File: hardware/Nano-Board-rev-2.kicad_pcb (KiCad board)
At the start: 2 copper layers, 125.7 x 53 mm, 75 parts, among them J1 Conn_01x02_Pin, J2 USB_B_Micro, J3 Conn_02x05_Odd_Even, J4 Conn_02x05_Odd_Even, J5 Conn_02x05_Odd_Even, J6 Micro_SD_Card_Det1, P1 Conn_02x05_Odd_Even, P2 Conn_02x05_Odd_Even, P3 Conn_02x05_Odd_Even, U1 STM32F303CCTx, U4 CDSOT236-0504C, U5 TLV75733PDBV, U6 STLINK-V3MODS, U8 MPU6050, Y1 8MHz Crystal

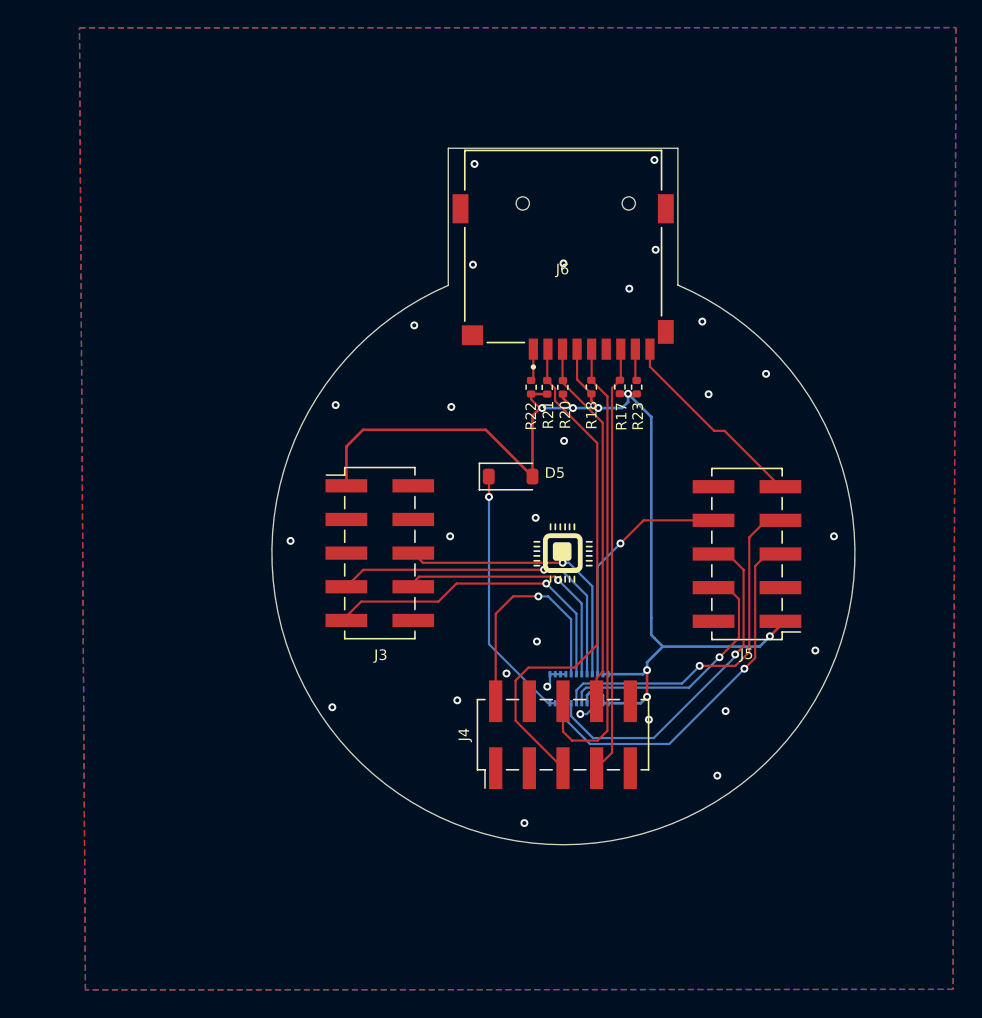
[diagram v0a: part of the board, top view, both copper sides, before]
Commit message: hardware: prune auxiliary libraries and refresh PCB
Delete vendor footprint/symbol bundles that were lying around
hardware/ as reference imports — none of them are used by
Nano-Board-rev-2.kicad_pcb directly:

  - 1x2_Hea/, FPC/, MPU-6050/, SAMTEC-SMH_1x2/,
    USB/, USB MICRO/, USB MICRO 4 NANO/, XKB_microSD.pretty/,
    fp/, stlink-v3mods_cad/
  - LDO/ sub-project (separate board, doesn't belong here)
  - one-off helpers: how-to-import.htm at various paths,
    fabrication-toolkit-options.json, nano (2).csv,
    Backup.gitignore.txt
  - cached pre-built 3D models under hardware/3d/ (KiCad regenerates
    them on demand)

The PCB itself is updated.
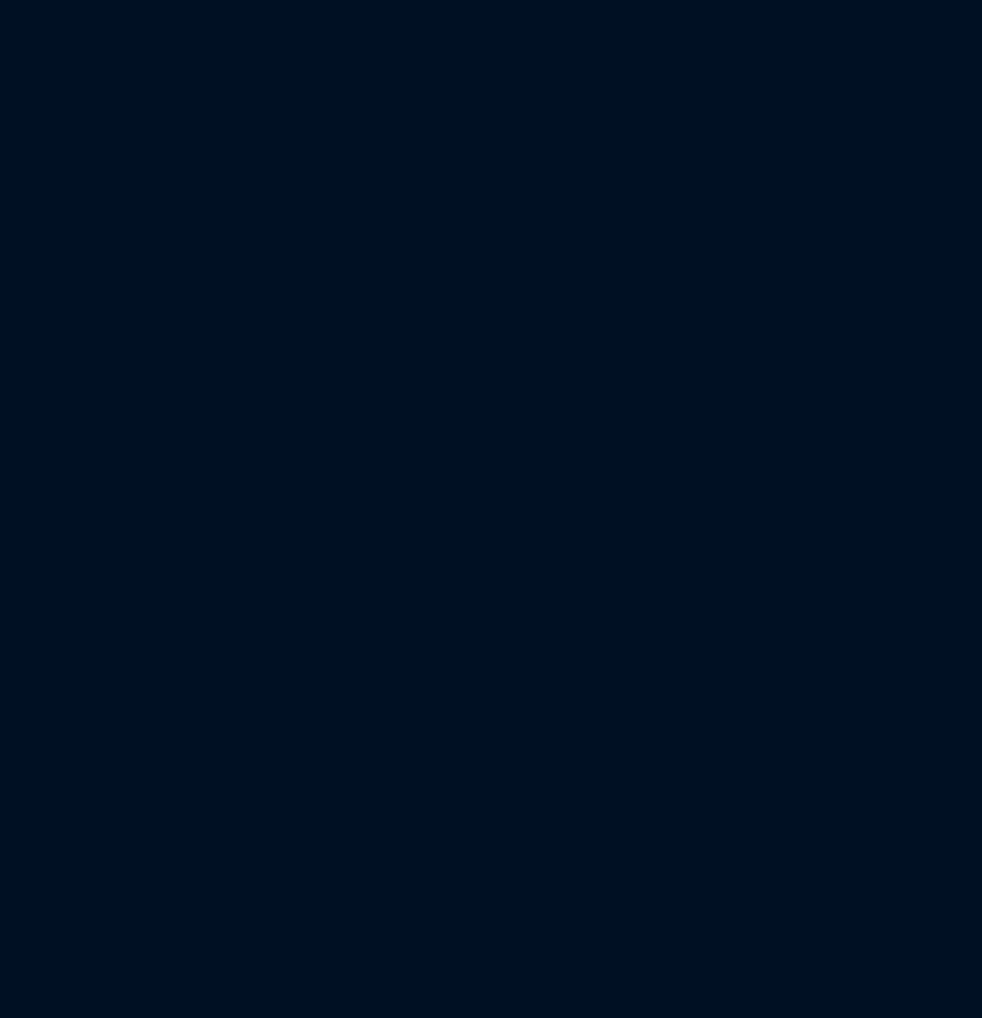
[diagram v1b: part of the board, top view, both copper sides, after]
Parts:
- removed D5: 1N5819WS, Diode_SMD:D_SOD-123
- removed the G*** at (177.5, 111.8)
- removed the G*** at (173.3, 83.4)
- removed J3, J4, J5: Conn_02x05_Odd_Even, Connector_PinHeader_2.54mm:PinHeader_2x05_P2.54mm_Vertical_SMD
- removed J6: Micro_SD_Card_Det1, fp:CUI_MSD-1-A
- removed R17, R18, R20, R21, R22, R23: 10K, Resistor_SMD:R_0402_1005Metric
- removed U3: ~, FPC_CONNECTOR24:OK-24F024-04
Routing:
- net +3.3V: track 86.3 -> 0.00 mm, vias 7 -> 0
- net SD_CS: track 39.2 -> 0.00 mm
- net SD_SCL: track 35.5 -> 0.00 mm
- net SD_MISO: track 32.2 -> 0.00 mm
- net TP_IN: track 28.2 -> 0.00 mm, vias 1 -> 0
- net SD_MOSI: track 28.0 -> 0.00 mm
- net TP_SDA: track 26.8 -> 0.00 mm, vias 1 -> 0
- net TP_SCL: track 26.2 -> 0.00 mm, vias 1 -> 0
- net LCD_SCL: track 25.4 -> 0.00 mm, vias 1 -> 0
- net LCD_MOSI: track 24.2 -> 0.00 mm, vias 1 -> 0
- net LCD_CSX: track 21.2 -> 0.00 mm, vias 1 -> 0
- net TP_RST: track 19.6 -> 0.00 mm, vias 1 -> 0
- net Net-(D5-K): track 19.5 -> 0.00 mm, vias 1 -> 0
- net LCD_MISO: track 19.4 -> 0.00 mm, vias 1 -> 0
- net LCD_RST: track 18.3 -> 0.00 mm, vias 1 -> 0
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- removed copper zone on B.Cu, net GND1
- removed copper zone on F.Cu, net GND1
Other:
- board size 125.7 x 53 mm -> 44 x 52.6 mm
- board text removed: "Nano LCD Shield"
- board text removed: "µSD Card"

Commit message: hardware prune auxiliary libraries and refresh PCB
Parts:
- removed BOOT: SW3, Button_Switch_SMD:SW_Tactile_SPST_NO_Straight_CK_PTS636Sx25SMTRLFS
- removed C1, C11, C15, C18, C2, C20, C21, C3: 100nF, Capacitor_SMD:C_0402_1005Metric
- removed C10, C17, C7, C8: 1uF, Capacitor_SMD:C_0402_1005Metric
- removed C19: 2.2nF, Capacitor_SMD:C_0402_1005Metric
- removed C4: 4.7uF, Capacitor_SMD:C_0402_1005Metric
- removed C5, C6: 20pF, Capacitor_SMD:C_0402_1005Metric
- removed C9: 10nF, Capacitor_SMD:C_0402_1005Metric
- removed D1, D4: RED LED, LED_SMD:LED_0603_1608Metric
- removed D2: BLUE LED, LED_SMD:LED_0603_1608Metric
- removed D3: GREEN LED, LED_SMD:LED_0603_1608Metric
- removed D6, D7: 1N5819WS, Diode_SMD:D_SOD-123
- removed G*** (x2): LOGO, newdemo.preety:nano
- removed H1, H2, H3, H4: MountingHole, MountingHole:MountingHole_2.2mm_M2
- removed J1: Conn_01x02_Pin, Connector_PinSocket_2.54mm:PinSocket_1x02_P2.54mm_Vertical
- removed J2: USB_B_Micro, FB_Library:micro_USB
- removed P1, P2, P3: Conn_02x05_Odd_Even, Connector_PinSocket_2.54mm:PinSocket_2x05_P2.54mm_Vertical_SMD
- removed R1, R14, R15, R16, R2, R9: 330, Resistor_SMD:R_0402_1005Metric
- removed R10, R11: 2.2K, Resistor_SMD:R_0402_1005Metric
- removed R12, R3: 100, Resistor_SMD:R_0402_1005Metric
- removed R13, R19, R4, R8: 10K, Resistor_SMD:R_0402_1005Metric
- removed R25: 0, Resistor_SMD:R_0603_1608Metric
- removed R5, R6: 20, Resistor_SMD:R_0402_1005Metric
- removed R7: 1.5K, Resistor_SMD:R_0402_1005Metric
- removed RESET: SW1, Button_Switch_SMD:SW_Tactile_SPST_NO_Straight_CK_PTS636Sx25SMTRLFS
- removed U1: STM32F303CCTx, Package_QFP:LQFP-48_7x7mm_P0.5mm
- removed U4: CDSOT236-0504C, Package_TO_SOT_SMD:SOT-23-6
- removed U5: TLV75733PDBV, Package_TO_SOT_SMD:SOT-23-5
- removed U6: STLINK-V3MODS, model:MODULE_STLINK-V3MODS
- removed U8: MPU6050, Footprint:Mpu6050
- removed USER: SW2, Button_Switch_SMD:SW_Tactile_SPST_NO_Straight_CK_PTS636Sx25SMTRLFS
- removed Y1: 8MHz Crystal, Crystal:Crystal_SMD_HC49-SD
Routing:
- net +3V3: track 190.4 -> 0.00 mm, vias 11 -> 0
- net LED_2: track 70.7 -> 0.00 mm, vias 2 -> 0
- net +5V: track 49.2 -> 0.00 mm, vias 4 -> 0
- net RESET: track 48.1 -> 0.00 mm, vias 3 -> 0
- net USART1_TX: track 42.4 -> 0.00 mm, vias 3 -> 0
- net USER_BTN: track 40.2 -> 0.00 mm, vias 1 -> 0
- net USART1_RX: track 35.3 -> 0.00 mm, vias 3 -> 0
- net I2C1_SDA: track 33.8 -> 0.00 mm, vias 2 -> 0
- net SWDIO: track 33.0 -> 0.00 mm
- net USB_DM: track 32.7 -> 0.00 mm, vias 1 -> 0
- net USB_DP: track 32.7 -> 0.00 mm, vias 1 -> 0
- net LED_3: track 32.4 -> 0.00 mm, vias 1 -> 0
- net MPU_INT: track 32.4 -> 0.00 mm, vias 3 -> 0
- net LED_1: track 31.3 -> 0.00 mm, vias 1 -> 0
- net PA7: track 28.9 -> 0.00 mm, vias 1 -> 0
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- removed copper zone on B.Cu, net GND
- removed copper zone on F.Cu, net GND
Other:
- board outline removed
- board text removed: "+5V"
- board text removed: "+X"
- board text removed: "+Y"
- board text removed: "+Z"
- board text removed: "."
- board text removed: "10"
- board text removed: "2"
- board text removed: "9"
- board text removed: "FASTBIT EMBEDDED"
- board text removed: "GND"
- board text removed: "nano-v3.0"
- board text removed: "www.fastbitembedded.com"

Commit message: feat: add Three.js PCB 3D viewer with auto-deploy via GitHub Pages
- Add config/web/3d-viewer.html: custom Three.js viewer with OrbitControls,
  GLTFLoader+Meshopt, RoomEnvironment, ACES tonemapping, three-light rig,
  soft shadows; top/bottom/reset/background buttons, loading spinner with
  progress, file:// error fallback, mobile-responsive UI
- Add scripts/convert_to_glb.py: kicad-cli pcb export glb wrapper
- feature-push.yml: convert PCB to GLB, compress with gltf-transform
  (Meshopt + webp), render viewer template, link from landing page
- Restore PCB layout
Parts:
- added BOOT: SW3, Button_Switch_SMD:SW_Tactile_SPST_NO_Straight_CK_PTS636Sx25SMTRLFS, F.Cu at (131.6, 114.8)
- added C1: 100nF, Capacitor_SMD:C_0402_1005Metric, B.Cu at (116.0, 117.5)
- added C10: 1uF, Capacitor_SMD:C_0402_1005Metric, F.Cu at (114.1, 82.9)
- added C11: 100nF, Capacitor_SMD:C_0402_1005Metric, F.Cu at (107.5, 85.7)
- added C15: 100nF, Capacitor_SMD:C_0402_1005Metric, B.Cu at (130.2, 115.1)
- added C17: 1uF, Capacitor_SMD:C_0402_1005Metric, B.Cu at (124.3, 112.6)
- added C18: 100nF, Capacitor_SMD:C_0402_1005Metric, F.Cu at (119.7, 98.3)
- added C19: 2.2nF, Capacitor_SMD:C_0402_1005Metric, F.Cu at (115.7, 100.4)
- added C2: 100nF, Capacitor_SMD:C_0402_1005Metric, B.Cu at (112.6, 108.7)
- added C20: 100nF, Capacitor_SMD:C_0402_1005Metric, F.Cu at (122.3, 101.0)
- added C21: 100nF, Capacitor_SMD:C_0402_1005Metric, B.Cu at (106.6, 114.0)
- added C3: 100nF, Capacitor_SMD:C_0402_1005Metric, B.Cu at (124.3, 108.1)
- added C4: 4.7uF, Capacitor_SMD:C_0402_1005Metric, B.Cu at (121.0, 105.9)
- added C5: 20pF, Capacitor_SMD:C_0402_1005Metric, B.Cu at (129.1, 102.2)
- added C6: 20pF, Capacitor_SMD:C_0402_1005Metric, B.Cu at (129.1, 104.3)
- added C7: 1uF, Capacitor_SMD:C_0402_1005Metric, F.Cu at (135.0, 94.2)
- added C8: 1uF, Capacitor_SMD:C_0402_1005Metric, F.Cu at (133.7, 88.6)
- added C9: 10nF, Capacitor_SMD:C_0402_1005Metric, B.Cu at (125.4, 112.6)
- added D1: RED LED, LED_SMD:LED_0603_1608Metric, F.Cu at (128.7, 84.7)
- added D2: BLUE LED, LED_SMD:LED_0603_1608Metric, F.Cu at (139.0, 104.0)
- added D3: GREEN LED, LED_SMD:LED_0603_1608Metric, F.Cu at (99.1, 102.8)
- added D4: RED LED, LED_SMD:LED_0603_1608Metric, F.Cu at (119.0, 122.5)
- added D5: 1N5819WS, Diode_SMD:D_SOD-123, F.Cu at (196.6, 95.5)
- added D6: 1N5819WS, Diode_SMD:D_SOD-123, F.Cu at (122.8, 82.0)
- added D7: 1N5819WS, Diode_SMD:D_SOD-123, F.Cu at (125.4, 82.0)
- added G***: LOGO, newdemo.preety:nano, F.Cu at (200.6, 101.2)
- added G***: LOGO, newdemo.preety:nano, F.Cu at (118.9, 91.5)
- added G***: LOGO, newdemo.preety:SD_C, B.Cu at (196.3, 72.8)
- added G***: LOGO, newdemo.preety:nano, B.Cu at (104.2, 98.6)
- added H1: MountingHole, MountingHole:MountingHole_2.2mm_M2, F.Cu at (109.0, 111.0)
- added H2: MountingHole, MountingHole:MountingHole_2.2mm_M2, F.Cu at (128.5, 111.3)
- added H3: MountingHole, MountingHole:MountingHole_2.2mm_M2, F.Cu at (107.7, 92.4)
- added H4: MountingHole, MountingHole:MountingHole_2.2mm_M2, F.Cu at (130.2, 92.3)
- added J1: Conn_01x02_Pin, Connector_PinSocket_2.54mm:PinSocket_1x02_P2.54mm_Vertical, F.Cu at (105.4, 87.2)
- added J2: USB_B_Micro, FB_Library:micro_USB, F.Cu at (121.5, 73.4)
- added J3: Conn_02x05_Odd_Even, Connector_PinHeader_2.54mm:PinHeader_2x05_P2.54mm_Vertical_SMD, F.Cu at (186.7, 101.2)
- added J4: Conn_02x05_Odd_Even, Connector_PinHeader_2.54mm:PinHeader_2x05_P2.54mm_Vertical_SMD, F.Cu at (200.6, 114.9)
- added J5: Conn_02x05_Odd_Even, Connector_PinHeader_2.54mm:PinHeader_2x05_P2.54mm_Vertical_SMD, F.Cu at (214.4, 101.3)
- added J6: Micro_SD_Card_Det1, fp:CUI_MSD-1-A, F.Cu at (200.6, 78.1)
- added P1: Conn_02x05_Odd_Even, Connector_PinSocket_2.54mm:PinSocket_2x05_P2.54mm_Vertical_SMD, F.Cu at (132.8, 101.8)
- added P2: Conn_02x05_Odd_Even, Connector_PinSocket_2.54mm:PinSocket_2x05_P2.54mm_Vertical_SMD, F.Cu at (118.9, 115.4)
- added P3: Conn_02x05_Odd_Even, Connector_PinSocket_2.54mm:PinSocket_2x05_P2.54mm_Vertical_SMD, F.Cu at (105.1, 101.7)
- added R1: 330, Resistor_SMD:R_0402_1005Metric, F.Cu at (128.7, 88.1)
- added R10: 2.2K, Resistor_SMD:R_0402_1005Metric, F.Cu at (115.7, 102.3)
- added R11: 2.2K, Resistor_SMD:R_0402_1005Metric, F.Cu at (114.7, 102.3)
- added R12: 100, Resistor_SMD:R_0402_1005Metric, B.Cu at (106.2, 115.7)
- added R13: 10K, Resistor_SMD:R_0402_1005Metric, B.Cu at (104.8, 114.4)
- added R14: 330, Resistor_SMD:R_0402_1005Metric, F.Cu at (102.1, 110.9)
- added R15: 330, Resistor_SMD:R_0402_1005Metric, F.Cu at (99.1, 100.1)
- added R16: 330, Resistor_SMD:R_0402_1005Metric, F.Cu at (119.5, 121.0)
- added R17: 10K, Resistor_SMD:R_0402_1005Metric, F.Cu at (204.9, 88.7)
- added R18: 10K, Resistor_SMD:R_0402_1005Metric, F.Cu at (202.7, 88.7)
- added R19: 10K, Resistor_SMD:R_0402_1005Metric, F.Cu at (117.2, 121.1)
- added R2: 330, Resistor_SMD:R_0402_1005Metric, F.Cu at (139.0, 101.3)
- added R20: 10K, Resistor_SMD:R_0402_1005Metric, F.Cu at (200.5, 88.7)
- added R21: 10K, Resistor_SMD:R_0402_1005Metric, F.Cu at (199.4, 88.7)
- added R22: 10K, Resistor_SMD:R_0402_1005Metric, F.Cu at (198.1, 88.7)
- added R23: 10K, Resistor_SMD:R_0402_1005Metric, F.Cu at (206.1, 88.7)
- added R25: 0, Resistor_SMD:R_0603_1608Metric, F.Cu at (116.0, 85.5)
- added R3: 100, Resistor_SMD:R_0402_1005Metric, B.Cu at (131.7, 113.6)
- added R4: 10K, Resistor_SMD:R_0402_1005Metric, F.Cu at (113.0, 82.9)
- added R5: 20, Resistor_SMD:R_0402_1005Metric, F.Cu at (121.4, 86.3)
- added R6: 20, Resistor_SMD:R_0402_1005Metric, F.Cu at (120.4, 86.3)
- added R7: 1.5K, Resistor_SMD:R_0402_1005Metric, F.Cu at (122.4, 86.3)
- added R8: 10K, Resistor_SMD:R_0402_1005Metric, B.Cu at (131.8, 115.5)
- added R9: 330, Resistor_SMD:R_0402_1005Metric, F.Cu at (127.3, 119.4)
- added RESET: SW1, Button_Switch_SMD:SW_Tactile_SPST_NO_Straight_CK_PTS636Sx25SMTRLFS, F.Cu at (112.8, 76.5)
- added U1: STM32F303CCTx, Package_QFP:LQFP-48_7x7mm_P0.5mm, B.Cu at (118.4, 111.5)
- added U3: ~, FPC_CONNECTOR24:OK-24F024-04, B.Cu at (201.9, 108.8)
- added U4: CDSOT236-0504C, Package_TO_SOT_SMD:SOT-23-6, F.Cu at (118.9, 82.5)
- added U5: TLV75733PDBV, Package_TO_SOT_SMD:SOT-23-5, F.Cu at (134.5, 91.5)
- added U6: STLINK-V3MODS, model:MODULE_STLINK-V3MODS, B.Cu at (118.9, 72.6)
- added U8: MPU6050, Footprint:Mpu6050, F.Cu at (118.9, 101.7)
- added USER: SW2, Button_Switch_SMD:SW_Tactile_SPST_NO_Straight_CK_PTS636Sx25SMTRLFS, F.Cu at (106.1, 114.7)
- added Y1: 8MHz Crystal, Crystal:Crystal_SMD_HC49-SD, B.Cu at (133.1, 103.2)
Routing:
- net +3V3: track 0.00 -> 190.4 mm, vias 0 -> 11
- net +3.3V: track 0.00 -> 86.3 mm, vias 0 -> 7
- net LED_2: track 0.00 -> 70.7 mm, vias 0 -> 2
- net +5V: track 0.00 -> 49.2 mm, vias 0 -> 4
- net RESET: track 0.00 -> 48.1 mm, vias 0 -> 3
- net USART1_TX: track 0.00 -> 42.4 mm, vias 0 -> 3
- net USER_BTN: track 0.00 -> 40.2 mm, vias 0 -> 1
- net SD_CS: track 0.00 -> 39.2 mm
- net SD_SCL: track 0.00 -> 35.5 mm
- net USART1_RX: track 0.00 -> 35.3 mm, vias 0 -> 3
- net I2C1_SDA: track 0.00 -> 33.8 mm, vias 0 -> 2
- net SWDIO: track 0.00 -> 33.0 mm
- net USB_DM: track 0.00 -> 32.7 mm, vias 0 -> 1
- net USB_DP: track 0.00 -> 32.7 mm, vias 0 -> 1
- net LED_3: track 0.00 -> 32.4 mm, vias 0 -> 1
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- added copper zone on B.Cu, net GND
- added copper zone on F.Cu, net GND
- added copper zone on B.Cu, net GND1
- added copper zone on F.Cu, net GND1
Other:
- board outline added: 125.7 x 53 mm
- board text added: "+5V"
- board text added: "+X"
- board text added: "+Y"
- board text added: "+Z"
- board text added: "."
- board text added: "10"
- board text added: "2"
- board text added: "9"
- board text added: "FASTBIT EMBEDDED"
- board text added: "GND"
- board text added: "Nano LCD Shield"
- board text added: "nano-v3.0"
- board text added: "www.fastbitembedded.com"
- board text added: "µSD Card"
